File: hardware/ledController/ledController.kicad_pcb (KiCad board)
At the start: 2 copper layers, 5 parts, among them IC1 PIC16F1769-I_ML, J1 Conn_01x06

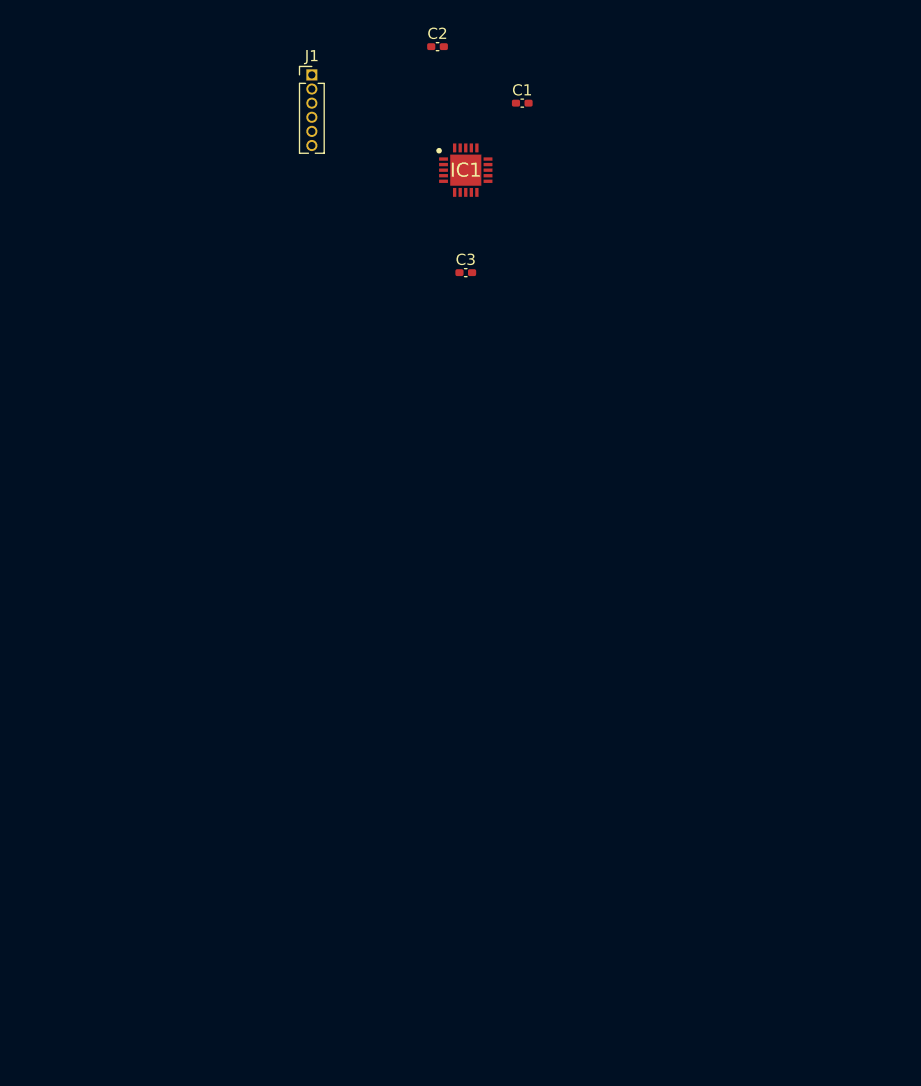
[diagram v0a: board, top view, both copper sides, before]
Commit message: First attempt of schematic to PCB
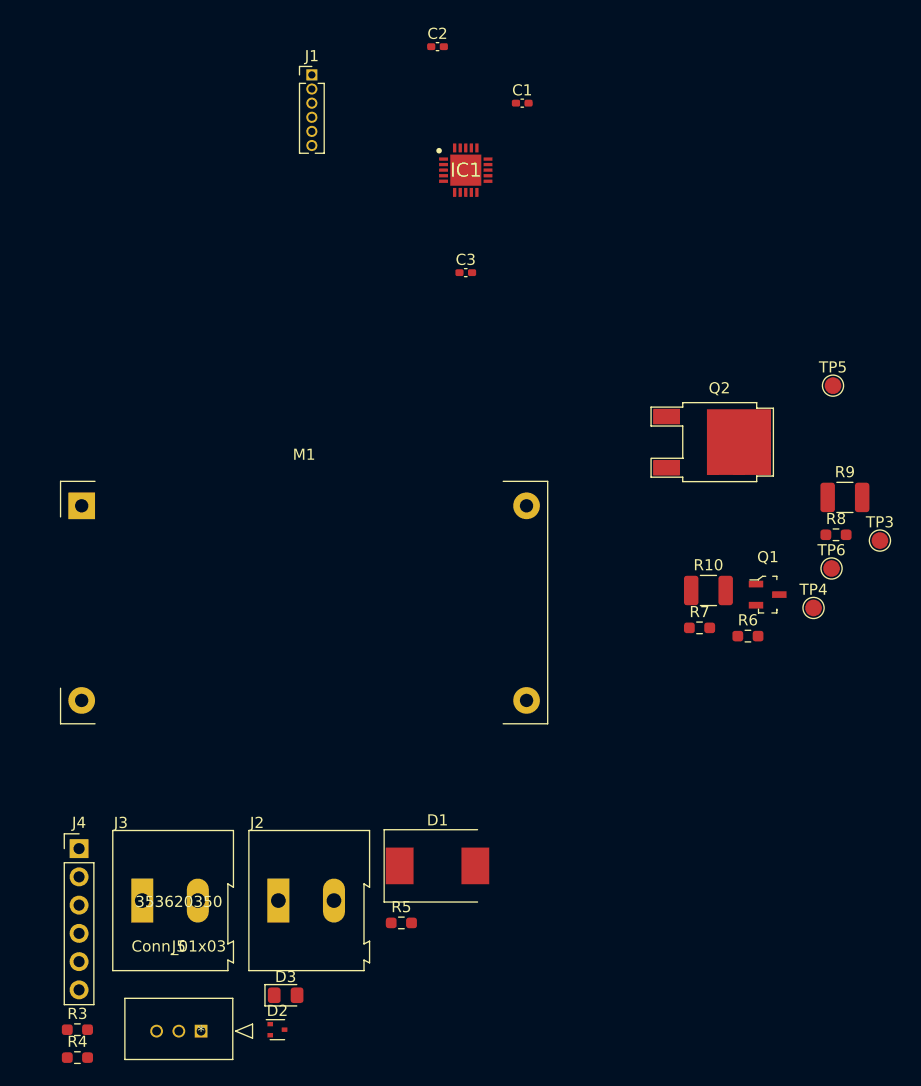
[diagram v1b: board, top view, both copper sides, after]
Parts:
- added D1: B340, Diode_SMD:D_SMC, F.Cu at (142.2, 142.2)
- added D2: RCLAMP0502BA, Package_TO_SOT_SMD:SOT-523, F.Cu at (127.8, 157.0)
- added D3: LED_G, LED_SMD:LED_0805_2012Metric_Pad1.15x1.40mm_HandSolder, F.Cu at (128.6, 153.9)
- added J2: Screw_Terminal_01x02, TerminalBlock:TerminalBlock_Altech_AK300-2_P5.00mm, F.Cu at (127.9, 145.4)
- added J3: Screw_Terminal_01x02, TerminalBlock:TerminalBlock_Altech_AK300-2_P5.00mm, F.Cu at (115.7, 145.4)
- added J4: Conn_01x06, Connector_PinHeader_2.54mm:PinHeader_1x06_P2.54mm_Vertical, F.Cu at (110.0, 140.7)
- added J5: Conn_01x03, molex-footprints:353620350, F.Cu at (121.0, 157.1)
- added M1: LM2596_module, ym-footprints:LM2596_module, F.Cu at (130.2, 117.9)
- added Q1: FMMT458TA, digikey-footprints:SOT-23-3, F.Cu at (171.9, 117.8)
- added Q2: BUJ302AD, ym-footprints:SOT-428, F.Cu at (167.6, 104.1)
- added R10: 1, Resistor_SMD:R_1210_3225Metric_Pad1.30x2.65mm_HandSolder, F.Cu at (166.6, 117.5)
- added R3: 200K, Resistor_SMD:R_0603_1608Metric_Pad0.98x0.95mm_HandSolder, F.Cu at (109.9, 157.0)
- added R4: 10K, Resistor_SMD:R_0603_1608Metric_Pad0.98x0.95mm_HandSolder, F.Cu at (109.9, 159.5)
- added R5: 2.4K, Resistor_SMD:R_0603_1608Metric_Pad0.98x0.95mm_HandSolder, F.Cu at (139.0, 147.4)
- added R6: 200, Resistor_SMD:R_0603_1608Metric_Pad0.98x0.95mm_HandSolder, F.Cu at (170.2, 121.6)
- added R7: 20K, Resistor_SMD:R_0603_1608Metric_Pad0.98x0.95mm_HandSolder, F.Cu at (165.8, 120.8)
- added R8: 10K, Resistor_SMD:R_0603_1608Metric_Pad0.98x0.95mm_HandSolder, F.Cu at (178.1, 112.5)
- added R9: 1, Resistor_SMD:R_1210_3225Metric_Pad1.30x2.65mm_HandSolder, F.Cu at (178.9, 109.1)
- added TP3: TestPoint, TestPoint:TestPoint_Pad_D1.5mm, F.Cu at (182.0, 113.0)
- added TP4: TestPoint, TestPoint:TestPoint_Pad_D1.5mm, F.Cu at (176.1, 119.0)
- added TP5: TestPoint, TestPoint:TestPoint_Pad_D1.5mm, F.Cu at (177.8, 99.1)
- added TP6: TestPoint, TestPoint:TestPoint_Pad_D1.5mm, F.Cu at (177.7, 115.5)
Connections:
- C1 pad 1: Net-(C1-Pad1) -> /~{MCLKR}
- IC1 pad 1: unconnected-(IC1-Pad1) -> /~{MCLKR}
- IC1 pad 10: unconnected-(IC1-Pad10) -> /OPA-FB
- IC1 pad 11: unconnected-(IC1-Pad11) -> /OPA-OUT
- IC1 pad 20: unconnected-(IC1-Pad20) -> /COMM-TX
- IC1 pad 4: unconnected-(IC1-Pad4) -> /V_{IN}
- IC1 pad 6: unconnected-(IC1-Pad6) -> Net-(D3-Pad2)
- IC1 pad 9: unconnected-(IC1-Pad9) -> /COMM-RX
- J1 pad 1: Net-(C1-Pad1) -> /~{MCLKR}

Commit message: PCB work
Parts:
- added C4: 1000p, Capacitor_SMD:C_0402_1005Metric_Pad0.74x0.62mm_HandSolder, F.Cu at (130.6, 116.4)
- added H1: MountingHole, MountingHole:MountingHole_2.5mm_Pad_TopBottom, F.Cu at (141.0, 111.0)
- added H2: MountingHole, MountingHole:MountingHole_2.5mm_Pad_TopBottom, F.Cu at (136.0, 149.0)
- added R1: 1K, Resistor_SMD:R_0603_1608Metric_Pad0.98x0.95mm_HandSolder, F.Cu at (130.1, 112.2)
- added R2: 50K, Resistor_SMD:R_0603_1608Metric_Pad0.98x0.95mm_HandSolder, F.Cu at (131.0, 114.9)
- added TP1: TestPoint, ym-footprints:TestPoint_Pad_0.185in_x_0.135in, F.Cu at (131.8, 135.0)
- J5: value Conn_01x03 -> Conn_01x02_Male; footprint molex-footprints:353620350 -> Connector_PinSocket_2.54mm:PinSocket_1x02_P2.54mm_Vertical
- M1, Q1: moved to B.Cu
- TP6: footprint TestPoint:TestPoint_Pad_D1.5mm -> ym-footprints:TestPoint_Pad_0.185in_x_0.135in; moved to B.Cu
- moved TP6 70.3 mm to (110.1, 134.8), turned to 180 degrees
- moved J5 49.4 mm to (150.2, 117.2), turned to 180 degrees
- moved C2 46.9 mm to (121.2, 110.5), turned to 180 degrees
- moved C1 46.7 mm to (118.2, 108.0), turned to 180 degrees
- moved TP3 46.6 mm to (135.9, 119.6)
- moved R9 45.5 mm to (139.0, 131.0), turned to 180 degrees
- moved TP4 44.5 mm to (138.0, 142.0)
- moved TP5 42.6 mm to (145.0, 126.2)
- moved R8 42.5 mm to (136.9, 123.0)
- moved IC1 42.3 mm to (124.5, 116.8)
- moved R3 40.3 mm to (117.1, 117.3)
- moved R4 39.7 mm to (117.2, 120.5), turned to 180 degrees
- moved R6 38.5 mm to (131.7, 119.6)
- moved J1 36.5 mm to (121.6, 106.4), turned to 90 degrees
- moved Q2 35.2 mm to (149.0, 134.0)
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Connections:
- D1 pad 2: Net-(D1-Pad2) -> /V_{IN}
- IC1 pad 12: unconnected-(IC1-Pad12) -> /SENSE-OUT
- IC1 pad 4: /V_{IN} -> /V_{MEAS}
- J2 pad 2: Net-(D1-Pad2) -> /V_{IN}
- J5 pad 1: GND -> /SENSE-OUT
- J5 pad 2: /PIR-OUT -> GND
- R3 pad 2: /V_{IN} -> /V_{MEAS}
- R4 pad 1: /V_{IN} -> /V_{MEAS}
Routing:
- net +3.3V: track 0.00 -> 50.7 mm, vias 0 -> 1
- net VDC: track 0.00 -> 48.5 mm
- net /SENSE-OUT: track 0.00 -> 28.0 mm
- net Net-(Q1-Pad1): track 0.00 -> 26.2 mm, vias 0 -> 1
- net Net-(Q2-Pad3): track 0.00 -> 25.8 mm
- net /COMM-TX: track 0.00 -> 23.0 mm, vias 0 -> 2
- net /LED_driver/LED-N: track 0.00 -> 19.2 mm, vias 0 -> 1
- net /COMM-RX: track 0.00 -> 17.2 mm
- net /OPA-FB: track 0.00 -> 15.7 mm
- net /~{MCLKR}: track 0.00 -> 14.2 mm
- net /PGC: track 0.00 -> 11.2 mm
- net /PGD: track 0.00 -> 10.5 mm
- net GND: track 0.00 -> 8.17 mm, vias 0 -> 53
- net /V_{MEAS}: track 0.00 -> 7.57 mm
- net Net-(Q1-Pad2): track 0.00 -> 6.65 mm, vias 0 -> 1
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- added copper zone on F.Cu, net /V_{IN}
- added copper zone on B.Cu, net GND
- added copper zone on F.Cu, net GND
- added copper zone on F.Cu, net VDC
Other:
- board outline added: 50 x 50 mm
- board text added: "12V"
- board text added: "IN+"
- board text added: "IN-"
- board text added: "LED Controller Board V1.0"
- board text added: "LED-OUT"
- board text added: "OUT+"
- board text added: "OUT-"
- board text added: "Prog"
- board text added: "Rx"
- board text added: "SENSE"
- board text added: "Tx"
- board text added: "UART"

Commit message: Minor changes
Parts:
- moved C4 28.8 mm to (140.7, 89.4)
- moved J1 28.8 mm to (131.8, 79.4)
- moved R10 28.8 mm to (149.1, 109.3)
- moved R2 28.8 mm to (141.1, 87.9)
- moved IC1 28.8 mm to (134.6, 89.9)
- moved C2 28.8 mm to (131.4, 83.6)
- moved C3 28.8 mm to (136.2, 83.6)
- moved D1 28.8 mm to (137.1, 120.0)
- moved D2 28.8 mm to (133.1, 107.4)
- moved D3 28.8 mm to (134.1, 95.0)
- moved H1 28.8 mm to (151.1, 84.0)
- moved H2 28.8 mm to (146.1, 122.0)
- moved J4 28.8 mm to (141.5, 102.0)
- moved J5 28.8 mm to (160.3, 90.3)
- moved M1 28.8 mm to (140.4, 90.9)
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
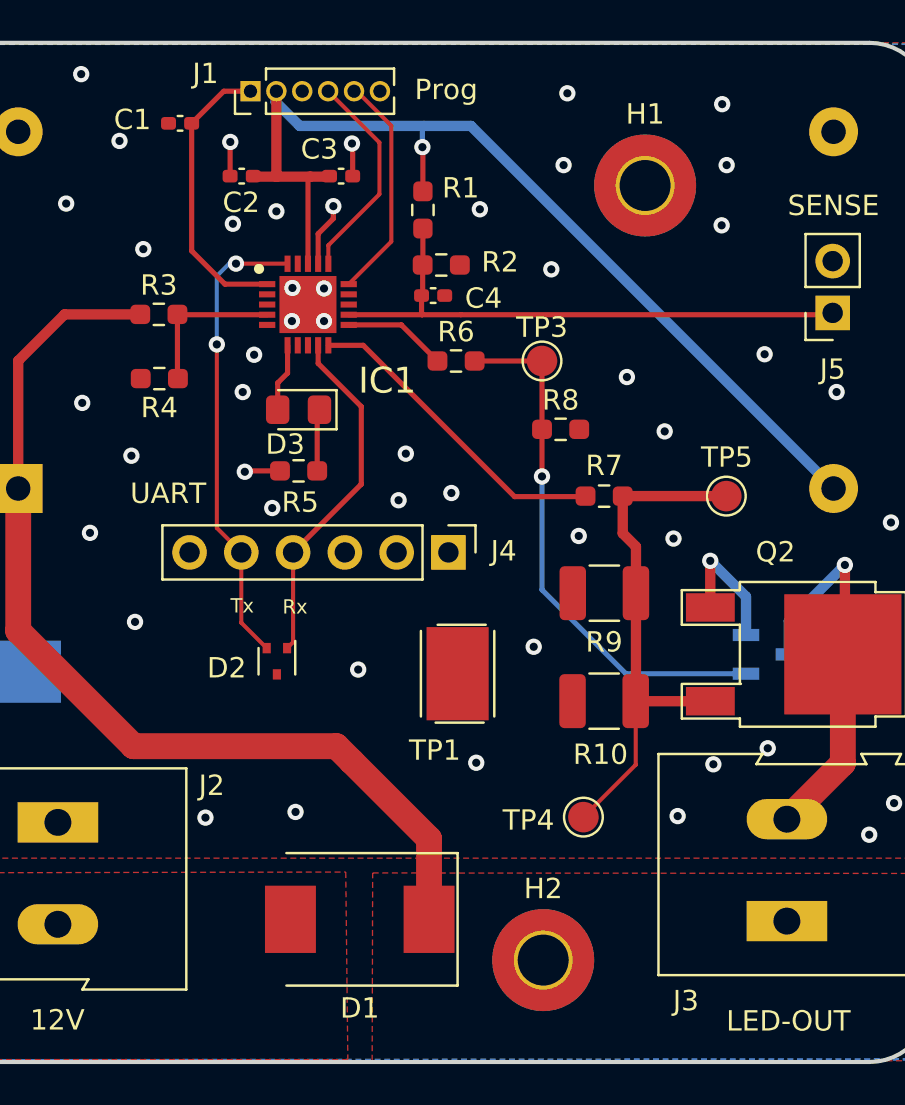
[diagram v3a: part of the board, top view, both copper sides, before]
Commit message: Changed based on the footprint updates
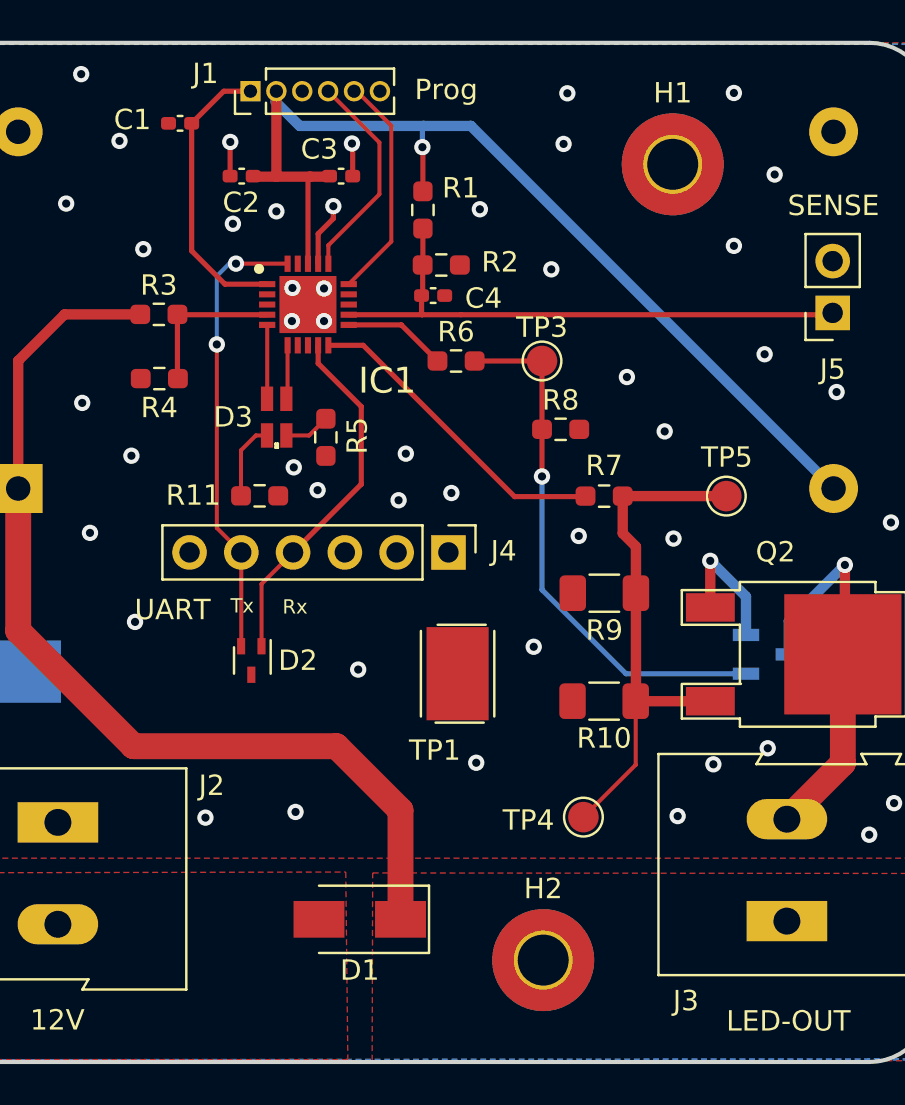
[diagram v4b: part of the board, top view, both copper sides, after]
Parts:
- added R11: 2.4K, Resistor_SMD:R_0603_1608Metric_Pad0.98x0.95mm_HandSolder, F.Cu at (132.2, 99.3)
- D1: footprint Diode_SMD:D_SMC -> Diode_SMD:D_SMA
- D2: footprint Package_TO_SOT_SMD:SOT-523 -> ym-footprints:SC-75
- D3: value LED_G -> LED_Dual_AKKA; footprint LED_SMD:LED_0805_2012Metric_Pad1.15x1.40mm_HandSolder -> LED_SMD:LED_Kingbright_APHBM2012_2x1.25mm
- R10, R9: footprint Resistor_SMD:R_1210_3225Metric_Pad1.30x2.65mm_HandSolder -> Resistor_SMD:R_1206_3216Metric_Pad1.30x1.75mm_HandSolder
- moved R5 2.12 mm to (135.5, 96.4), turned to -90 degrees
- moved H1 1.71 mm to (152.5, 83.0)
- moved D2 1.25 mm to (131.8, 107.3), turned to 180 degrees
- moved D3 1.13 mm to (133.1, 95.4), turned to 0 degrees
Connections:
- D3 pad 1: Net-(D3-Pad1) -> Net-(IC1-Pad5)
- IC1 pad 5: unconnected-(IC1-Pad5) -> Net-(IC1-Pad5)
- IC1 pad 6: Net-(D3-Pad2) -> Net-(IC1-Pad6)
- R5 pad 1: Net-(D3-Pad1) -> Net-(R5-Pad1)
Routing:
- net Net-(IC1-Pad5): track 0.00 -> 3.63 mm
- net Net-(D3-Pad1): track 3.05 -> 0.00 mm
- net Net-(IC1-Pad6): track 0.00 -> 2.65 mm
- net Net-(R5-Pad1): track 0.00 -> 2.28 mm
- net GND: track 8.17 -> 6.43 mm, vias 53 -> 51
- net /COMM-TX: track 23.0 -> 22.4 mm
- net VDC: track 48.5 -> 47.9 mm
